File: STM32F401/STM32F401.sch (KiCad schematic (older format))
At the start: 56 parts, among them U1 STM32F401CCUx, U2 MCP73832-2-OT, U3 MCP1811A-033TT, Y1 Crystal_GND24_Small, Y2 Crystal_Small

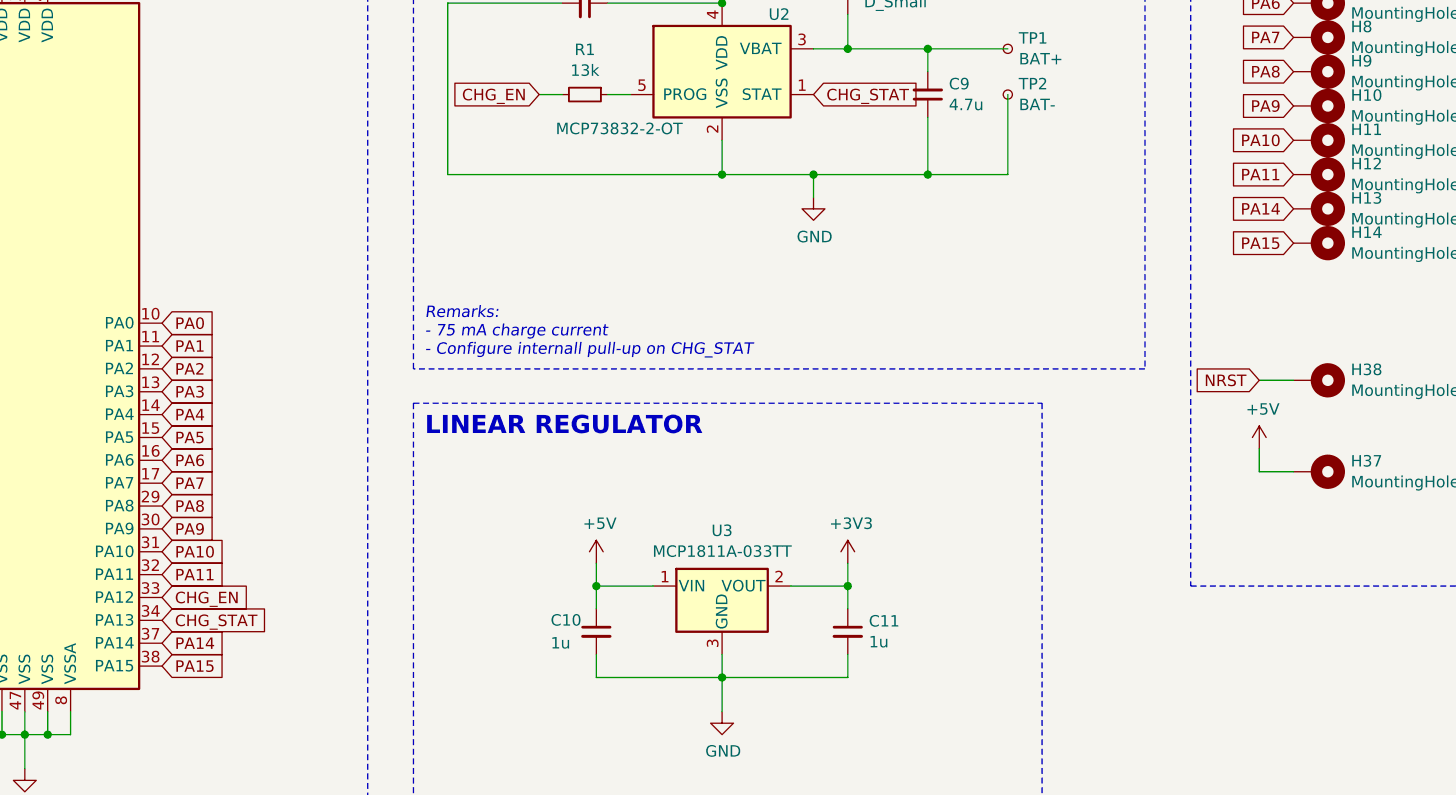
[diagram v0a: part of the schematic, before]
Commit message: Swap `PA13` with `PA11`
Use `PA11` as the `CHG_STAT` pin to free up `PA13` which is needed for
SWD.
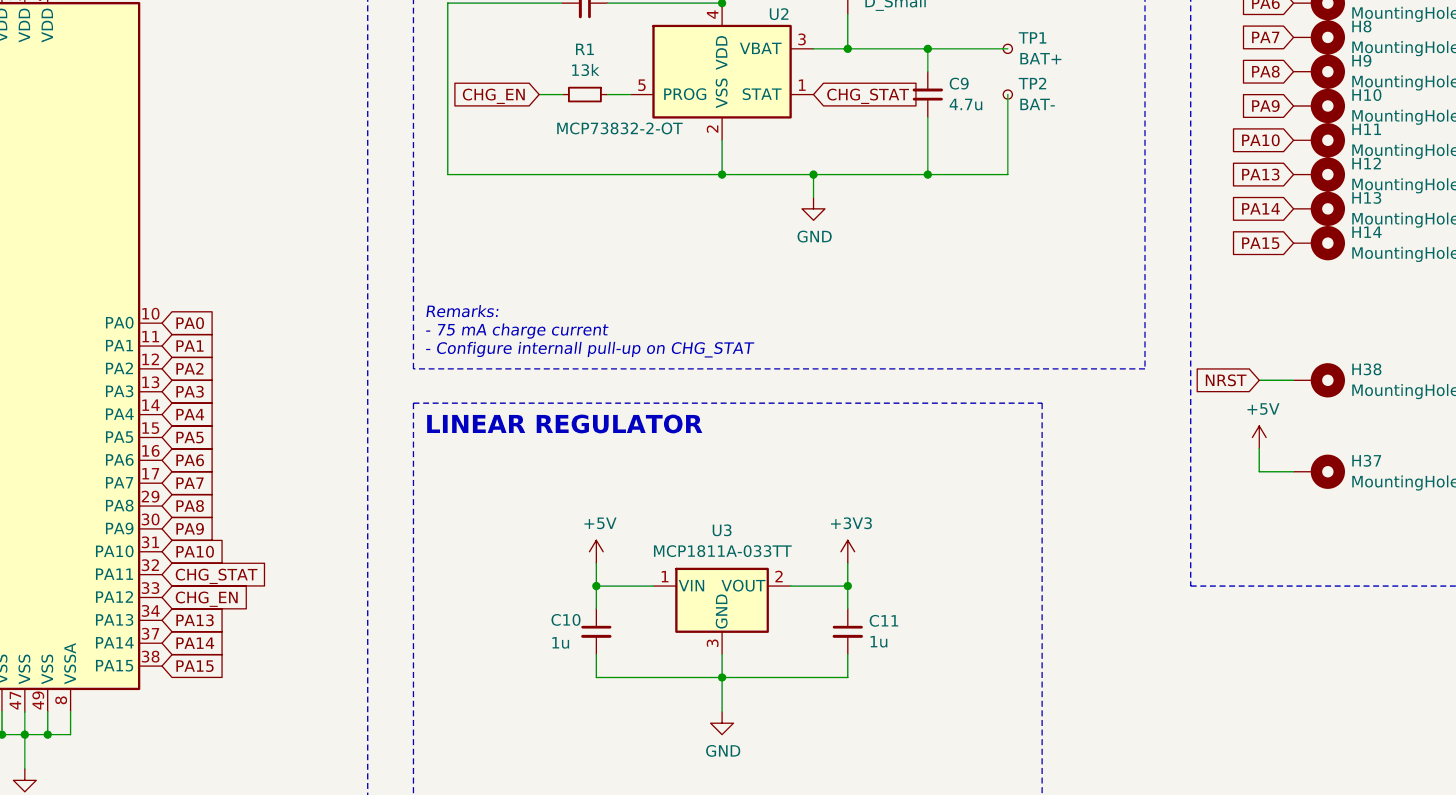
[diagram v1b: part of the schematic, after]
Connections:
- net CHG_STAT: now also U1.32 (PA11); no longer U1.34 (PA13)
- net PA11 renamed PA13
- net PA13: now also U1.34 (PA13); no longer U1.32 (PA11)
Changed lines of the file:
@@
 Text GLabel 3500 4250 2    50   Input ~ 0
 PA10
-Text GLabel 3500 4350 2    50   Input ~ 0
-PA11
+Text GLabel 3500 4550 2    50   Input ~ 0
+PA13
 Text GLabel 3500 4650 2    50   Input ~ 0
 PA14
@@
 PA10
 Text GLabel 8450 2600 0    50   Input ~ 0
-PA11
+PA13
 Text GLabel 8450 2750 0    50   Input ~ 0
 PA14
@@
 Text GLabel 3500 4450 2    50   Input ~ 0
 CHG_EN
-Text GLabel 3500 4550 2    50   Input ~ 0
+Text GLabel 3500 4350 2    50   Input ~ 0
 CHG_STAT
 Wire Wire Line
